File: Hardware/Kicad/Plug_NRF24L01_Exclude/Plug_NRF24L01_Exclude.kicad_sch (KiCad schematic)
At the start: 38 parts, among them J1 Conn_01x07_Socket, J2 Conn_01x08_Socket, J2 Conn_02x07_Odd_Even, Q1 2N7002, Q2 2N7002, Q3 2N7002, SW2 SW_SPST, U2 MIC5219-3.3YMM, U3 STM32L412KBTx

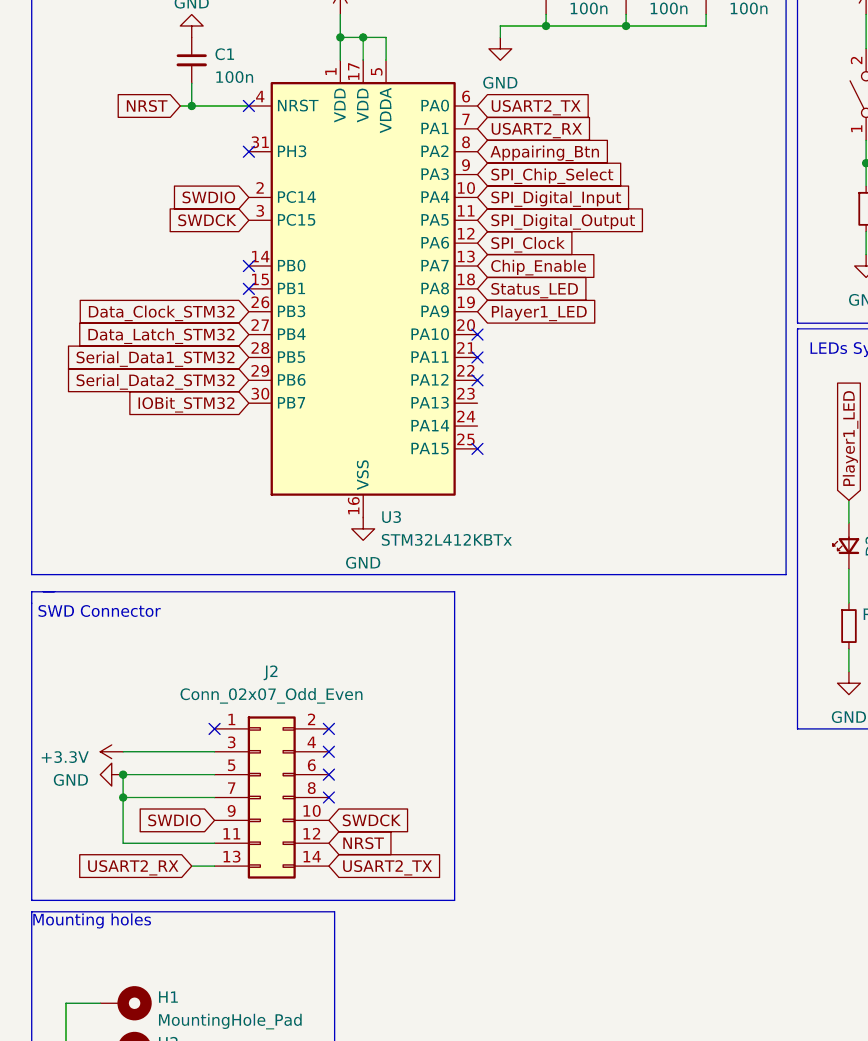
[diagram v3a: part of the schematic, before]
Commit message: Updated Plug_NRF24L01_Exclude (V1.1) - PCB (Routing) / Schematic (Pins assignment)
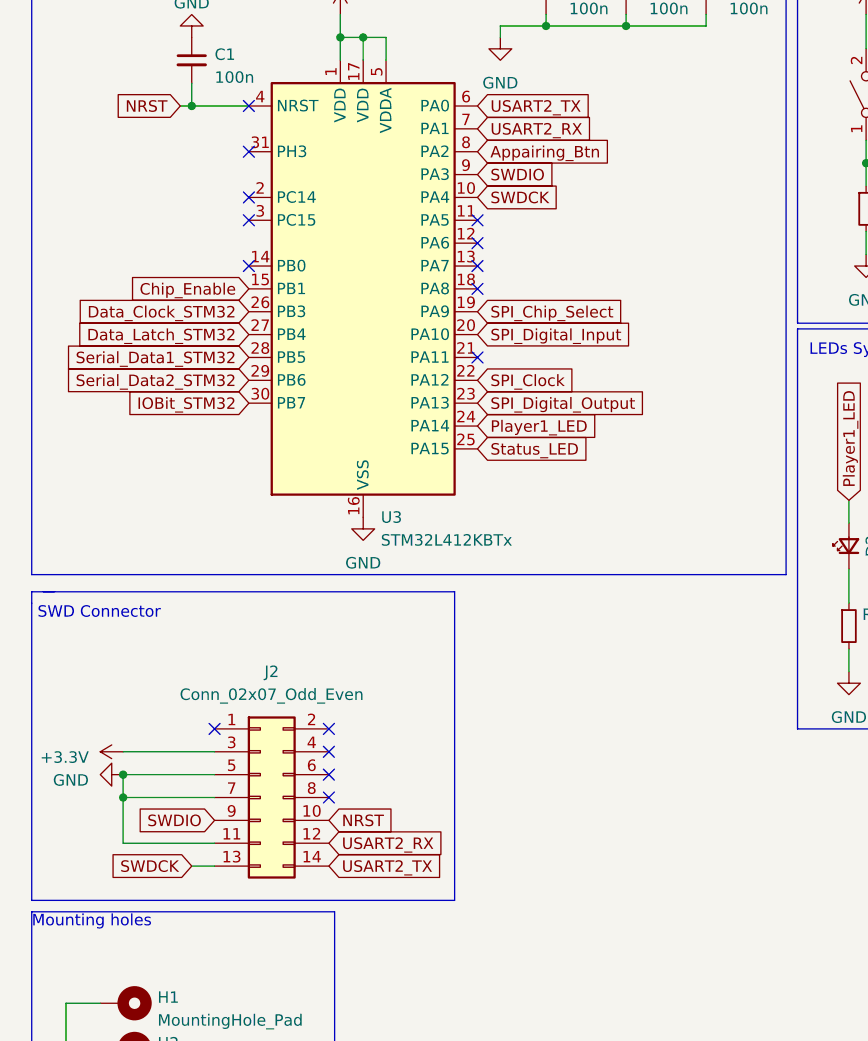
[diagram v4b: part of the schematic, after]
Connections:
- net Chip_Enable: now also U3.15 (PB1); no longer U3.13 (PA7)
- net NRST: now also J2.10 (Pin_10); no longer J2.12 (Pin_12)
- net Player1_LED: now also U3.24 (PA14); no longer U3.19 (PA9)
- net SPI_Chip_Select: now also U3.19 (PA9); no longer U3.9 (PA3)
- net SPI_Clock: now also U3.22 (PA12); no longer U3.12 (PA6)
- net SPI_Digital_Input: now also U3.20 (PA10); no longer U3.10 (PA4)
- net SPI_Digital_Output: now also U3.23 (PA13); no longer U3.11 (PA5)
- net SWDCK: now also J2.13 (Pin_13), U3.10 (PA4); no longer J2.10 (Pin_10), U3.3 (PC15)
- net SWDIO: now also U3.9 (PA3); no longer U3.2 (PC14)
- net Status_LED: now also U3.25 (PA15); no longer U3.18 (PA8)
- net USART2_RX: now also J2.12 (Pin_12); no longer J2.13 (Pin_13)
- no-connect marks 15 -> 17
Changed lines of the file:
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@@
   )
   (no_connect (at 180.34 113.03))
-  (no_connect (at 66.04 74.93))
+  (no_connect (at 40.64 46.99))
+  (no_connect (at 40.64 49.53))
+  (no_connect (at 66.04 52.07))
   (no_connect (at 40.64 36.83))
-  (no_connect (at 66.04 64.77))
   (no_connect (at 186.055 69.85))
   (no_connect (at 36.83 106.045))
-  (no_connect (at 66.04 67.31))
+  (no_connect (at 66.04 57.15))
+  (no_connect (at 66.04 64.77))
   (no_connect (at 49.53 106.045))
   (no_connect (at 49.53 108.585))
   (no_connect (at 49.53 111.125))
   (no_connect (at 40.64 54.61))
-  (no_connect (at 40.64 57.15))
   (no_connect (at 40.64 41.91))
+  (no_connect (at 66.04 54.61))
+  (no_connect (at 66.04 49.53))
   (no_connect (at 49.53 113.665))
-  (no_connect (at 66.04 62.23))
   (wire (pts (xy 205.105 118.745) (xy 205.105 123.825))
     (stroke (width 0) (type default))
@@
     (effects (font (size 1.27 1.27)) (justify left bottom))
   )
-  (global_label "SWDIO" (shape input) (at 40.64 46.99 180) (fields_autoplaced)
-    (effects (font (size 1.27 1.27)) (justify right))
-    (property "Intersheetrefs" "${INTERSHEET_REFS}" (at 31.868 46.99 0)
-      (effects (font (size 1.27 1.27)) (justify right) hide)
+  (global_label "SWDCK" (shape input) (at 66.04 46.99 0) (fields_autoplaced)
+    (effects (font (size 1.27 1.27)) (justify left))
+    (property "Intersheetrefs" "${INTERSHEET_REFS}" (at 75.4167 46.99 0)
+      (effects (font (size 1.27 1.27)) (justify left) hide)
     )
   )
@@
     )
   )
-  (global_label "SPI_Digital_Output" (shape input) (at 66.04 49.53 0) (fields_autoplaced)
-    (effects (font (size 1.27 1.27)) (justify left))
-    (property "Intersheetrefs" "${INTERSHEET_REFS}" (at 86.3627 49.53 0)
-      (effects (font (size 1.27 1.27)) (justify left) hide)
-    )
-  )
-  (global_label "SWDCK" (shape input) (at 49.53 116.205 0) (fields_autoplaced)
-    (effects (font (size 1.27 1.27)) (justify left))
-    (property "Intersheetrefs" "${INTERSHEET_REFS}" (at 58.9067 116.205 0)
-      (effects (font (size 1.27 1.27)) (justify left) hide)
+  (global_label "Chip_Enable" (shape input) (at 40.64 57.15 180) (fields_autoplaced)
+    (effects (font (size 1.27 1.27)) (justify right))
+    (property "Intersheetrefs" "${INTERSHEET_REFS}" (at 26.244 57.15 0)
+      (effects (font (size 1.27 1.27)) (justify right) hide)
     )
   )
@@
     )
   )
+  (global_label "Status_LED" (shape input) (at 66.04 74.93 0) (fields_autoplaced)
+    (effects (font (size 1.27 1.27)) (justify left))
+    (property "Intersheetrefs" "${INTERSHEET_REFS}" (at 79.3475 74.93 0)
+      (effects (font (size 1.27 1.27)) (justify left) hide)
+    )
+  )
   (global_label "Data_Latch_STM32" (shape input) (at 237.49 58.42 180) (fields_autoplaced)
     (effects (font (size 1.27 1.27)) (justify right))
@@
     )
   )
+  (global_label "Player1_LED" (shape input) (at 66.04 72.39 0) (fields_autoplaced)
+    (effects (font (size 1.27 1.27)) (justify left))
+    (property "Intersheetrefs" "${INTERSHEET_REFS}" (at 80.4966 72.39 0)
+      (effects (font (size 1.27 1.27)) (justify left) hide)
+    )
+  )
   (global_label "Data_Clock_SNES" (shape input) (at 261.62 35.56 0) (fields_autoplaced)
     (effects (font (size 1.27 1.27)) (justify left))
@@
     )
   )
-  (global_label "SPI_Digital_Input" (shape input) (at 66.04 46.99 0) (fields_autoplaced)
-    (effects (font (size 1.27 1.27)) (justify left))
-    (property "Intersheetrefs" "${INTERSHEET_REFS}" (at 84.9113 46.99 0)
+  (global_label "USART2_RX" (shape input) (at 49.53 118.745 0) (fields_autoplaced)
+    (effects (font (size 1.27 1.27)) (justify left))
+    (property "Intersheetrefs" "${INTERSHEET_REFS}" (at 62.9586 118.745 0)
       (effects (font (size 1.27 1.27)) (justify left) hide)
     )
@@
     )
   )
+  (global_label "SPI_Digital_Output" (shape input) (at 66.04 69.85 0) (fields_autoplaced)
+    (effects (font (size 1.27 1.27)) (justify left))
+    (property "Intersheetrefs" "${INTERSHEET_REFS}" (at 86.3627 69.85 0)
+      (effects (font (size 1.27 1.27)) (justify left) hide)
+    )
+  )
   (global_label "Data_Latch_SNES" (shape input) (at 261.62 58.42 0) (fields_autoplaced)
     (effects (font (size 1.27 1.27)) (justify left))
@@
     )
   )
+  (global_label "SPI_Digital_Input" (shape input) (at 66.04 62.23 0) (fields_autoplaced)
+    (effects (font (size 1.27 1.27)) (justify left))
+    (property "Intersheetrefs" "${INTERSHEET_REFS}" (at 84.9113 62.23 0)
+      (effects (font (size 1.27 1.27)) (justify left) hide)
+    )
+  )
   (global_label "USART2_RX" (shape input) (at 66.04 39.37 0) (fields_autoplaced)
     (effects (font (size 1.27 1.27)) (justify left))
@@
     )
   )
-  (global_label "NRST" (shape input) (at 49.53 118.745 0) (fields_autoplaced)
-    (effects (font (size 1.27 1.27)) (justify left))
-    (property "Intersheetrefs" "${INTERSHEET_REFS}" (at 57.2134 118.745 0)
+  (global_label "SPI_Chip_Select" (shape input) (at 66.04 59.69 0) (fields_autoplaced)
+    (effects (font (size 1.27 1.27)) (justify left))
+    (property "Intersheetrefs" "${INTERSHEET_REFS}" (at 84.0043 59.69 0)
       (effects (font (size 1.27 1.27)) (justify left) hide)
     )
@@
     )
   )
+  (global_label "SWDIO" (shape input) (at 66.04 44.45 0) (fields_autoplaced)
+    (effects (font (size 1.27 1.27)) (justify left))
+    (property "Intersheetrefs" "${INTERSHEET_REFS}" (at 74.812 44.45 0)
+      (effects (font (size 1.27 1.27)) (justify left) hide)
+    )
+  )
   (global_label "IOBit_STM32" (shape input) (at 40.64 69.85 180) (fields_autoplaced)
     (effects (font (size 1.27 1.27)) (justify right))
@@
     )
   )
-  (global_label "SWDCK" (shape input) (at 40.64 49.53 180) (fields_autoplaced)
-    (effects (font (size 1.27 1.27)) (justify right))
-    (property "Intersheetrefs" "${INTERSHEET_REFS}" (at 31.2633 49.53 0)
-      (effects (font (size 1.27 1.27)) (justify right) hide)
-    )
-  )
-  (global_label "Player1_LED" (shape input) (at 66.04 59.69 0) (fields_autoplaced)
-    (effects (font (size 1.27 1.27)) (justify left))
-    (property "Intersheetrefs" "${INTERSHEET_REFS}" (at 80.4966 59.69 0)
+  (global_label "SWDCK" (shape input) (at 34.29 121.285 180) (fields_autoplaced)
+    (effects (font (size 1.27 1.27)) (justify right))
+    (property "Intersheetrefs" "${INTERSHEET_REFS}" (at 24.9133 121.285 0)
+      (effects (font (size 1.27 1.27)) (justify right) hide)
+    )
+  )
+  (global_label "SPI_Clock" (shape input) (at 66.04 67.31 0) (fields_autoplaced)
+    (effects (font (size 1.27 1.27)) (justify left))
+    (property "Intersheetrefs" "${INTERSHEET_REFS}" (at 78.1986 67.31 0)
       (effects (font (size 1.27 1.27)) (justify left) hide)
     )
@@
     )
   )
-  (global_label "Chip_Enable" (shape input) (at 66.04 54.61 0) (fields_autoplaced)
-    (effects (font (size 1.27 1.27)) (justify left))
-    (property "Intersheetrefs" "${INTERSHEET_REFS}" (at 80.436 54.61 0)
+  (global_label "NRST" (shape input) (at 49.53 116.205 0) (fields_autoplaced)
+    (effects (font (size 1.27 1.27)) (justify left))
+    (property "Intersheetrefs" "${INTERSHEET_REFS}" (at 57.2134 116.205 0)
       (effects (font (size 1.27 1.27)) (justify left) hide)
     )
@@
     )
   )
-  (global_label "USART2_RX" (shape input) (at 34.29 121.285 180) (fields_autoplaced)
-    (effects (font (size 1.27 1.27)) (justify right))
-    (property "Intersheetrefs" "${INTERSHEET_REFS}" (at 20.8614 121.285 0)
-      (effects (font (size 1.27 1.27)) (justify right) hide)
-    )
-  )
   (global_label "Data_Latch_SNES" (shape input) (at 189.865 38.735 0) (fields_autoplaced)
     (effects (font (size 1.27 1.27)) (justify left))
@@
     )
   )
-  (global_label "SPI_Clock" (shape input) (at 66.04 52.07 0) (fields_autoplaced)
-    (effects (font (size 1.27 1.27)) (justify left))
-    (property "Intersheetrefs" "${INTERSHEET_REFS}" (at 78.1986 52.07 0)
-      (effects (font (size 1.27 1.27)) (justify left) hide)
-    )
-  )
   (global_label "NRST" (shape input) (at 33.02 36.83 180) (fields_autoplaced)
     (effects (font (size 1.27 1.27)) (justify right))
@@
     )
   )
-  (global_label "SPI_Chip_Select" (shape input) (at 66.04 44.45 0) (fields_autoplaced)
-    (effects (font (size 1.27 1.27)) (justify left))
-    (property "Intersheetrefs" "${INTERSHEET_REFS}" (at 84.0043 44.45 0)
-      (effects (font (size 1.27 1.27)) (justify left) hide)
-    )
-  )
   (global_label "Chip_Enable" (shape input) (at 189.865 77.47 0) (fields_autoplaced)
     (effects (font (size 1.27 1.27)) (justify left))
@@
       (effects (font (size 1.27 1.27)) (justify left) hide)
     )
-  )
-  (global_label "Status_LED" (shape input) (at 66.04 57.15 0) (fields_autoplaced)
-    (effects (font (size 1.27 1.27)) (justify left))
-    (property "Intersheetrefs" "${INTERSHEET_REFS}" (at 79.3475 57.15 0)
-      (effects (font (size 1.27 1.27)) (justify left) hide)
-    )
